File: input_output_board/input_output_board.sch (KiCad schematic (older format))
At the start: 20 parts, among them J1 Neutrik_NCJ6FA-H, J2 Neutrik_NCJ6FA-H, J3 Neutrik_NCJ6FA-H, J4 Neutrik_NCJ6FA-H, J5 AudioJack3, J6 Conn_02x05_Odd_Even, J7 Molex_SL_01x02_Male, J8 Molex_SL_01x02_Male, K1 G6S-2, K2 G6S-2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

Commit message: update input output board for headphone amp connections
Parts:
- added J6: Molex_SL_01x02_Male, Connector_Molex_SL:Molex_SL_A-70543-0001_1x02_P2.54mm_Vertical, symbol Connector_gkeeth:Molex_SL_01x02_Male
- added JP3, JP4: Jumper_NO_Small, Connector_PinHeader_2.54mm:PinHeader_1x02_P2.54mm_Vertical, symbol Device:Jumper_NO_Small
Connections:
- net labels added: headphone_cold, headphone_hot, headphone_select, main_cold, main_hot
- net labels removed: output_mute_select
- wire segments 141 -> 144
- no-connect marks 10 -> 8
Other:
- note added: "JP1 - JP4 optionally bypass K5\n\nTo hardwire main output:\nDNP K5, fit JP1 & JP3\n\nTo hardwire headphone output:\nDNP K5, fit JP2 & JP4"
- note added: "TODO\ncreate footprint for output jack\nmounting holes in corners?\npulldown resistors on J5?"
- note removed: "JP1 & JP2 optionally bypass K5\nif output relay is not required,\nDNP K5 and fit JP1 & JP2"
- note removed: "TODO\ncreate footprint for output jack\nmounting holes in corners?\nGND normally open terminals on K5? through resistor?"
- moved on the sheet: J6, J7

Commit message: Update layout of input/output board
- remove jumpers to bypass output relay. Jumper wires can be soldered
onto relay footprint instead.
- layout of output connectors complete
- still need to finalize output connector choice & placement
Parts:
- removed JP1, JP2, JP3, JP4: Jumper_NO_Small, Connector_PinHeader_2.54mm:PinHeader_1x02_P2.54mm_Vertical, symbol Device:Jumper_NO_Small
- J7, J8: footprint Connector_Molex_SL:Molex_SL_A-70543-0001_1x02_P2.54mm_Vertical -> Connector_Molex_SL:Molex_SL_A-70553-0001_1x02_P2.54mm_Horizontal
- J9: renamed from J6; footprint Connector_Molex_SL:Molex_SL_A-70543-0001_1x02_P2.54mm_Vertical -> Connector_Molex_SL:Molex_SL_A-70553-0001_1x02_P2.54mm_Horizontal
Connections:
- wire segments 144 -> 136
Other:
- note removed: "JP1 - JP4 optionally bypass K5\n\nTo hardwire main output:\nDNP K5, fit JP1 & JP3\n\nTo hardwire headphone output:\nDNP K5, fit JP2 & JP4"
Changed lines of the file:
@@
 F 0 "J7" H 6322 4674 50  0000 R CNN
 F 1 "Molex_SL_01x02_Male" H 6322 4583 50  0000 R CNN
-F 2 "Connector_Molex_SL:Molex_SL_A-70543-0001_1x02_P2.54mm_Vertical" H 6350 4700 50  0001 C CNN
+F 2 "Connector_Molex_SL:Molex_SL_A-70553-0001_1x02_P2.54mm_Horizontal" H 6350 4700 50  0001 C CNN
 F 3 "https://www.molex.com/pdm_docs/sd/705430001_sd.pdf" H 6350 4700 50  0001 C CNN
 F 4 "Molex" H 6350 4700 50  0001 C CNN "Manufacturer"
@@
 $EndComp
 $Comp
-L Connector_gkeeth:Molex_SL_01x02_Male J6
+L Connector_gkeeth:Molex_SL_01x02_Male J9
 U 1 1 5D8346C7
 P 10000 2400
-F 0 "J6" H 10108 2167 50  0000 C CNN
+F 0 "J9" H 10108 2167 50  0000 C CNN
 F 1 "Molex_SL_01x02_Male" H 10108 2076 50  0000 C CNN
-F 2 "Connector_Molex_SL:Molex_SL_A-70543-0001_1x02_P2.54mm_Vertical" H 10000 2400 50  0001 C CNN
+F 2 "Connector_Molex_SL:Molex_SL_A-70553-0001_1x02_P2.54mm_Horizontal" H 10000 2400 50  0001 C CNN
 F 3 "https://www.molex.com/pdm_docs/sd/705430001_sd.pdf" H 10000 2400 50  0001 C CNN
 F 4 "Molex" H 10000 2400 50  0001 C CNN "Manufacturer"
@@
 $EndComp
 $Comp
-L power_gkeeth:GNDRELAY #PWR?
+L power_gkeeth:GNDRELAY #PWR0101
 U 1 1 5D821EF0
 P 9000 1150
-F 0 "#PWR?" H 9000 900 50  0001 C CNN
+F 0 "#PWR0101" H 9000 900 50  0001 C CNN
 F 1 "GNDRELAY" H 9004 995 50  0000 C CNN
 F 2 "" H 9000 1150 50  0001 C CNN
 F 3 "" H 9000 1150 50  0001 C CNN
 	1    9000 1150
-	1    0    0    -1
-$EndComp
-$Comp
-L Device:Jumper_NO_Small JP2
-U 1 1 5D821EEA
-P 9600 3250
-F 0 "JP2" H 9600 3343 50  0000 C CNN
-F 1 "Jumper_NO_Small" H 9600 3371 50  0001 C CNN
-F 2 "Connector_PinHeader_2.54mm:PinHeader_1x02_P2.54mm_Vertical" H 9600 3250 50  0001 C CNN
-F 3 "~" H 9600 3250 50  0001 C CNN
-	1    9600 3250
-	1    0    0    -1
-$EndComp
-Text Notes 7550 3650 0    50   ~ 0
-JP1 - JP4 optionally bypass K5\n\nTo hardwire main output:\nDNP K5, fit JP1 & JP3\n\nTo hardwire headphone output:\nDNP K5, fit JP2 & JP4
-$Comp
-L Device:Jumper_NO_Small JP1
-U 1 1 5D821ED4
-P 9600 3050
-F 0 "JP1" H 9600 3150 50  0000 C CNN
-F 1 "Jumper_NO_Small" H 9600 3171 50  0001 C CNN
-F 2 "Connector_PinHeader_2.54mm:PinHeader_1x02_P2.54mm_Vertical" H 9600 3050 50  0001 C CNN
-F 3 "~" H 9600 3050 50  0001 C CNN
-	1    9600 3050
 	1    0    0    -1
 $EndComp
@@
 F 0 "J8" H 7072 1974 50  0000 R CNN
 F 1 "Molex_SL_01x02_Male" H 7072 1883 50  0000 R CNN
-F 2 "Connector_Molex_SL:Molex_SL_A-70543-0001_1x02_P2.54mm_Vertical" H 7100 2000 50  0001 C CNN
+F 2 "Connector_Molex_SL:Molex_SL_A-70553-0001_1x02_P2.54mm_Horizontal" H 7100 2000 50  0001 C CNN
 F 3 "https://www.molex.com/pdm_docs/sd/705430001_sd.pdf" H 7100 2000 50  0001 C CNN
 F 4 "Molex" H 7100 2000 50  0001 C CNN "Manufacturer"
@@
 	9750 1400 9800 1400
 Connection ~ 8750 1050
-$Comp
-L Device:Jumper_NO_Small JP3
-U 1 1 5DA7C338
-P 9600 3500
-F 0 "JP3" H 9600 3600 50  0000 C CNN
-F 1 "Jumper_NO_Small" H 9600 3621 50  0001 C CNN
-F 2 "Connector_PinHeader_2.54mm:PinHeader_1x02_P2.54mm_Vertical" H 9600 3500 50  0001 C CNN
-F 3 "~" H 9600 3500 50  0001 C CNN
-	1    9600 3500
-	1    0    0    -1
-$EndComp
-$Comp
-L Device:Jumper_NO_Small JP4
-U 1 1 5DA7C8D9
-P 9600 3700
-F 0 "JP4" H 9600 3793 50  0000 C CNN
-F 1 "Jumper_NO_Small" H 9600 3821 50  0001 C CNN
-F 2 "Connector_PinHeader_2.54mm:PinHeader_1x02_P2.54mm_Vertical" H 9600 3700 50  0001 C CNN
-F 3 "~" H 9600 3700 50  0001 C CNN
-	1    9600 3700
-	1    0    0    -1
-$EndComp
 Text Label 8800 1900 0    50   ~ 0
 main_hot
@@
 Wire Wire Line
 	9450 2400 9800 2400
-Wire Wire Line
-	9000 3050 9500 3050
-Wire Wire Line
-	9000 3250 9500 3250
-Wire Wire Line
-	9000 3500 9500 3500
-Wire Wire Line
-	9000 3700 9500 3700
-Wire Wire Line
-	10350 3050 9700 3050
-Wire Wire Line
-	10350 3250 9700 3250
-Wire Wire Line
-	10350 3500 9700 3500
-Wire Wire Line
-	10350 3700 9700 3700
-Text Label 9000 3050 0    50   ~ 0
-output_hot
-Text Label 9000 3500 0    50   ~ 0
-output_cold
-Text Label 9000 3250 0    50   ~ 0
-output_hot
-Text Label 9000 3700 0    50   ~ 0
-output_cold
-Text Label 10350 3050 2    50   ~ 0
-main_hot
-Text Label 10350 3250 2    50   ~ 0
-headphone_hot
-Text Label 10350 3500 2    50   ~ 0
-main_cold
-Text Label 10350 3700 2    50   ~ 0
-headphone_cold
 Wire Notes Line
 	10450 550  5950 550

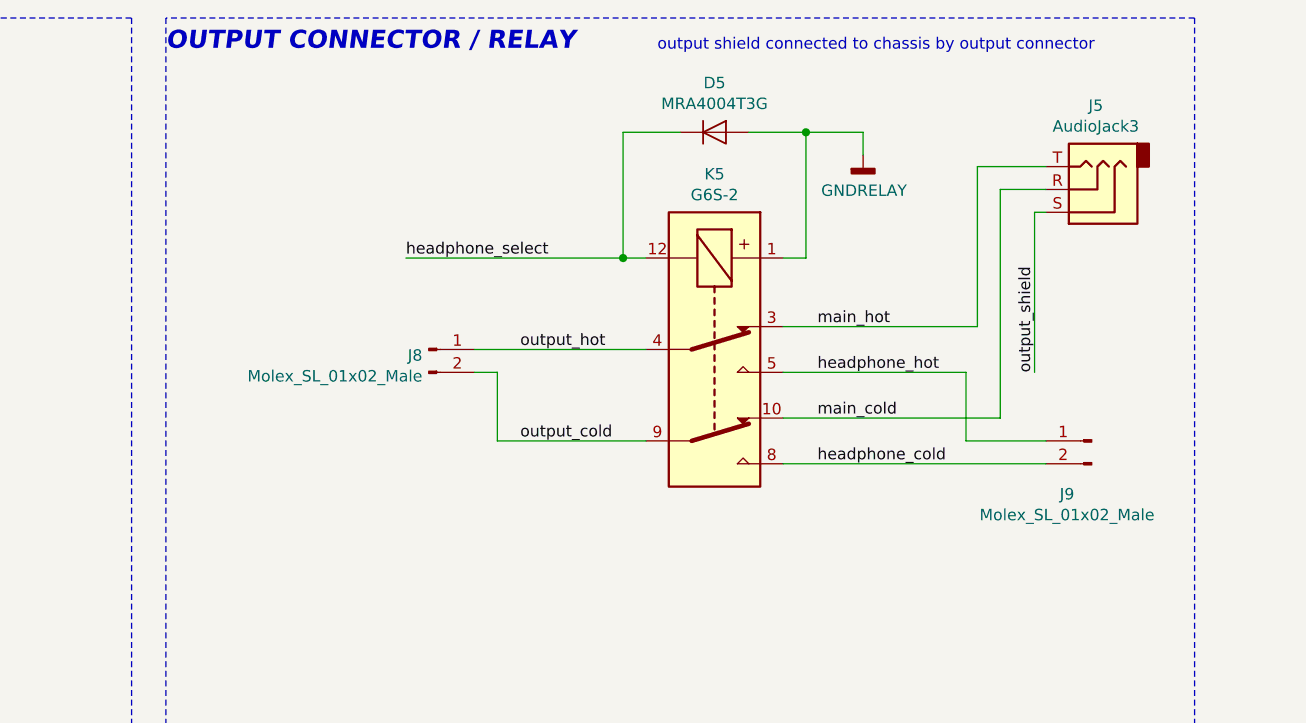
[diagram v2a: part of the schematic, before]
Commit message: update schematic & layout so output connector is same as input connectors
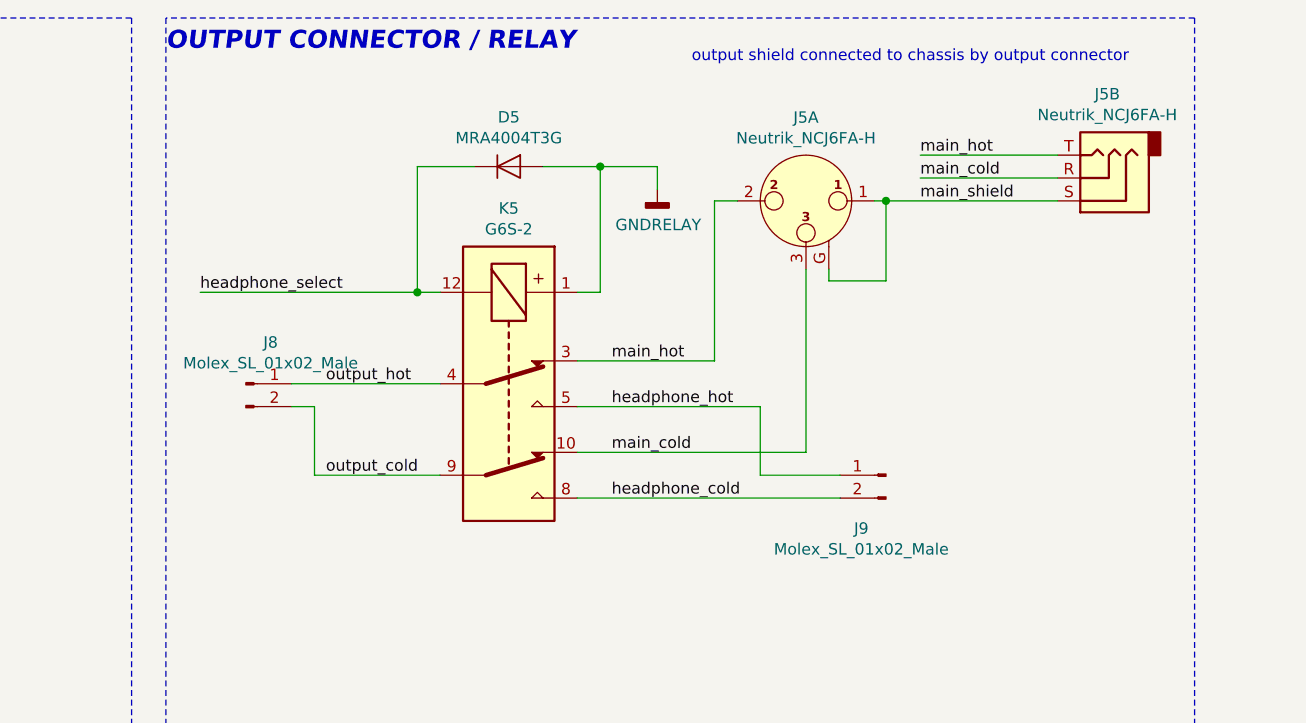
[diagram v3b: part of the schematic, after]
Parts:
- removed J5: AudioJack3, Connector_Audio:Jack_3.5mm_Neutrik_NMJ6HCD2_Horizontal, symbol Connector:AudioJack3
- added J5: Neutrik_NCJ6FA-H, Connector_Audio_gkeeth:Jack_Combo_Neutrik_NCJ6FA-H_Horizontal, symbol Connector_gkeeth:Neutrik_NCJ6FA-H
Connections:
- net main_cold: now also J5.3, J5.R
- net main_hot: now also J5.2, J5.T
- new net main_shield: J5.1, J5.G, J5.S
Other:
- moved on the sheet: D5, J8, J9, K5

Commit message: update schematic symbols to NCJ6FA-H-0 (no release tab), update footprints to project-local versions
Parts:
- J1, J2, J3, J4, J5: value Neutrik_NCJ6FA-H -> Neutrik_NCJ6FA-H-0; footprint Connector_Audio_gkeeth:Jack_Combo_Neutrik_NCJ6FA-H_Horizontal -> Connector_Audio_project:Jack_XLR-6.35mm_Neutrik_NCJ6FA-H-0_Horizontal; symbol Connector_gkeeth:Neutrik_NCJ6FA-H -> Connector_gkeeth:Neutrik_NCJ6FA-H-0
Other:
- note added: "TODO\nchange output jack to 6.35mm (not combo)\ncreate footprint for output jack\nmounting holes in corners?\npulldown resistors on J5?"
- note removed: "TODO\ncreate footprint for output jack\nmounting holes in corners?\npulldown resistors on J5?"
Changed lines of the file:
@@
 Tip: hot\nRing: cold\nSleeve: shield\n\n1: shield\n2: hot\n3: cold
 $Comp
-L Connector_gkeeth:Neutrik_NCJ6FA-H J2
+L Connector_gkeeth:Neutrik_NCJ6FA-H-0 J2
 U 1 1 5CAED56C
 P 2450 3450
 F 0 "J2" H 2450 3815 50  0000 C CNN
-F 1 "Neutrik_NCJ6FA-H" H 2450 3724 50  0000 C CNN
-F 2 "Connector_Audio_gkeeth:Jack_Combo_Neutrik_NCJ6FA-H_Horizontal" H 2450 3450 50  0001 C CNN
+F 1 "Neutrik_NCJ6FA-H-0" H 2450 3724 50  0000 C CNN
+F 2 "Connector_Audio_project:Jack_XLR-6.35mm_Neutrik_NCJ6FA-H-0_Horizontal" H 2450 3450 50  0001 C CNN
 F 3 "https://www.neutrik.com/media/8445/download/ncj6fa-v.pdf?v=1" H 2450 3450 50  0001 C CNN
 F 4 "Neutrik" H 2450 3450 50  0001 C CNN "Manufacturer"
@@
 $EndComp
 $Comp
-L Connector_gkeeth:Neutrik_NCJ6FA-H J2
+L Connector_gkeeth:Neutrik_NCJ6FA-H-0 J2
 U 2 1 5CAEF4BC
 P 1200 3350
 F 0 "J2" H 1182 2983 50  0000 C CNN
-F 1 "Neutrik_NCJ6FA-H" H 1182 3074 50  0000 C CNN
-F 2 "Connector_Audio_gkeeth:Jack_Combo_Neutrik_NCJ6FA-H_Horizontal" H 1200 3350 50  0001 C CNN
+F 1 "Neutrik_NCJ6FA-H-0" H 1182 3074 50  0000 C CNN
+F 2 "Connector_Audio_project:Jack_XLR-6.35mm_Neutrik_NCJ6FA-H-0_Horizontal" H 1200 3350 50  0001 C CNN
 F 3 "https://www.neutrik.com/media/8445/download/ncj6fa-v.pdf?v=1" H 1200 3350 50  0001 C CNN
 F 4 "Neutrik" H 1200 3350 50  0001 C CNN "Manufacturer"
@@
 Connection ~ 5000 5500
 $Comp
-L Connector_gkeeth:Neutrik_NCJ6FA-H J1
+L Connector_gkeeth:Neutrik_NCJ6FA-H-0 J1
 U 1 1 5CEE6A94
 P 2450 1700
 F 0 "J1" H 2450 2065 50  0000 C CNN
-F 1 "Neutrik_NCJ6FA-H" H 2450 1974 50  0000 C CNN
-F 2 "Connector_Audio_gkeeth:Jack_Combo_Neutrik_NCJ6FA-H_Horizontal" H 2450 1700 50  0001 C CNN
+F 1 "Neutrik_NCJ6FA-H-0" H 2450 1974 50  0000 C CNN
+F 2 "Connector_Audio_project:Jack_XLR-6.35mm_Neutrik_NCJ6FA-H-0_Horizontal" H 2450 1700 50  0001 C CNN
 F 3 "https://www.neutrik.com/media/8445/download/ncj6fa-v.pdf?v=1" H 2450 1700 50  0001 C CNN
 F 4 "Neutrik" H 2450 1700 50  0001 C CNN "Manufacturer"
@@
 $EndComp
 $Comp
-L Connector_gkeeth:Neutrik_NCJ6FA-H J1
+L Connector_gkeeth:Neutrik_NCJ6FA-H-0 J1
 U 2 1 5CEE74AE
 P 1200 1600
 F 0 "J1" H 1182 1233 50  0000 C CNN
-F 1 "Neutrik_NCJ6FA-H" H 1182 1324 50  0000 C CNN
-F 2 "Connector_Audio_gkeeth:Jack_Combo_Neutrik_NCJ6FA-H_Horizontal" H 1200 1600 50  0001 C CNN
+F 1 "Neutrik_NCJ6FA-H-0" H 1182 1324 50  0000 C CNN
+F 2 "Connector_Audio_project:Jack_XLR-6.35mm_Neutrik_NCJ6FA-H-0_Horizontal" H 1200 1600 50  0001 C CNN
 F 3 "https://www.neutrik.com/media/8445/download/ncj6fa-v.pdf?v=1" H 1200 1600 50  0001 C CNN
 F 4 "Neutrik" H 1200 1600 50  0001 C CNN "Manufacturer"
@@
 $EndComp
 $Comp
-L Connector_gkeeth:Neutrik_NCJ6FA-H J3
+L Connector_gkeeth:Neutrik_NCJ6FA-H-0 J3
 U 2 1 5CEE9005
 P 1200 5100
 F 0 "J3" H 1182 4733 50  0000 C CNN
-F 1 "Neutrik_NCJ6FA-H" H 1182 4824 50  0000 C CNN
-F 2 "Connector_Audio_gkeeth:Jack_Combo_Neutrik_NCJ6FA-H_Horizontal" H 1200 5100 50  0001 C CNN
+F 1 "Neutrik_NCJ6FA-H-0" H 1182 4824 50  0000 C CNN
+F 2 "Connector_Audio_project:Jack_XLR-6.35mm_Neutrik_NCJ6FA-H-0_Horizontal" H 1200 5100 50  0001 C CNN
 F 3 "https://www.neutrik.com/media/8445/download/ncj6fa-v.pdf?v=1" H 1200 5100 50  0001 C CNN
 F 4 "Neutrik" H 1200 5100 50  0001 C CNN "Manufacturer"
@@
 $EndComp
 $Comp
-L Connector_gkeeth:Neutrik_NCJ6FA-H J4
+L Connector_gkeeth:Neutrik_NCJ6FA-H-0 J4
 U 2 1 5CEE9880
 P 1200 6850
 F 0 "J4" H 1182 6483 50  0000 C CNN
-F 1 "Neutrik_NCJ6FA-H" H 1182 6574 50  0000 C CNN
-F 2 "Connector_Audio_gkeeth:Jack_Combo_Neutrik_NCJ6FA-H_Horizontal" H 1200 6850 50  0001 C CNN
+F 1 "Neutrik_NCJ6FA-H-0" H 1182 6574 50  0000 C CNN
+F 2 "Connector_Audio_project:Jack_XLR-6.35mm_Neutrik_NCJ6FA-H-0_Horizontal" H 1200 6850 50  0001 C CNN
 F 3 "https://www.neutrik.com/media/8445/download/ncj6fa-v.pdf?v=1" H 1200 6850 50  0001 C CNN
 F 4 "Neutrik" H 1200 6850 50  0001 C CNN "Manufacturer"
@@
 $EndComp
 $Comp
-L Connector_gkeeth:Neutrik_NCJ6FA-H J3
+L Connector_gkeeth:Neutrik_NCJ6FA-H-0 J3
 U 1 1 5CEEA018
 P 2450 5200
 F 0 "J3" H 2450 5565 50  0000 C CNN
-F 1 "Neutrik_NCJ6FA-H" H 2450 5474 50  0000 C CNN
-F 2 "Connector_Audio_gkeeth:Jack_Combo_Neutrik_NCJ6FA-H_Horizontal" H 2450 5200 50  0001 C CNN
+F 1 "Neutrik_NCJ6FA-H-0" H 2450 5474 50  0000 C CNN
+F 2 "Connector_Audio_project:Jack_XLR-6.35mm_Neutrik_NCJ6FA-H-0_Horizontal" H 2450 5200 50  0001 C CNN
 F 3 "https://www.neutrik.com/media/8445/download/ncj6fa-v.pdf?v=1" H 2450 5200 50  0001 C CNN
 F 4 "Neutrik" H 2450 5200 50  0001 C CNN "Manufacturer"
@@
 $EndComp
 $Comp
-L Connector_gkeeth:Neutrik_NCJ6FA-H J4
+L Connector_gkeeth:Neutrik_NCJ6FA-H-0 J4
 U 1 1 5CEEA75D
 P 2450 6950
 F 0 "J4" H 2450 7315 50  0000 C CNN
-F 1 "Neutrik_NCJ6FA-H" H 2450 7224 50  0000 C CNN
-F 2 "Connector_Audio_gkeeth:Jack_Combo_Neutrik_NCJ6FA-H_Horizontal" H 2450 6950 50  0001 C CNN
+F 1 "Neutrik_NCJ6FA-H-0" H 2450 7224 50  0000 C CNN
+F 2 "Connector_Audio_project:Jack_XLR-6.35mm_Neutrik_NCJ6FA-H-0_Horizontal" H 2450 6950 50  0001 C CNN
 F 3 "https://www.neutrik.com/media/8445/download/ncj6fa-v.pdf?v=1" H 2450 6950 50  0001 C CNN
 F 4 "Neutrik" H 2450 6950 50  0001 C CNN "Manufacturer"
@@
 input shield connected to chassis by input connector
 Text Notes 8200 6150 0    50   ~ 0
-TODO\ncreate footprint for output jack\nmounting holes in corners?\npulldown resistors on J5?
+TODO\nchange output jack to 6.35mm (not combo)\ncreate footprint for output jack\nmounting holes in corners?\npulldown resistors on J5?
 $Comp
 L power_gkeeth:GNDRELAY #PWR0102
@@
 	5000 5500 5000 7250
 $Comp
-L Connector_gkeeth:Neutrik_NCJ6FA-H J5
+L Connector_gkeeth:Neutrik_NCJ6FA-H-0 J5
 U 2 1 5D808DA8
 P 10050 1250
 F 0 "J5" H 10032 883 50  0000 C CNN
-F 1 "Neutrik_NCJ6FA-H" H 10032 974 50  0000 C CNN
-F 2 "Connector_Audio_gkeeth:Jack_Combo_Neutrik_NCJ6FA-H_Horizontal" H 10050 1250 50  0001 C CNN
+F 1 "Neutrik_NCJ6FA-H-0" H 10032 974 50  0000 C CNN
+F 2 "Connector_Audio_project:Jack_XLR-6.35mm_Neutrik_NCJ6FA-H-0_Horizontal" H 10050 1250 50  0001 C CNN
 F 3 "https://www.neutrik.com/media/8445/download/ncj6fa-v.pdf?v=1" H 10050 1250 50  0001 C CNN
 F 4 "Neutrik" H 10050 1250 50  0001 C CNN "Manufacturer"
@@
 $EndComp
 $Comp
-L Connector_gkeeth:Neutrik_NCJ6FA-H J5
+L Connector_gkeeth:Neutrik_NCJ6FA-H-0 J5
 U 1 1 5D807783
 P 8750 1350
 F 0 "J5" H 8750 1715 50  0000 C CNN
-F 1 "Neutrik_NCJ6FA-H" H 8750 1624 50  0000 C CNN
-F 2 "Connector_Audio_gkeeth:Jack_Combo_Neutrik_NCJ6FA-H_Horizontal" H 8750 1350 50  0001 C CNN
+F 1 "Neutrik_NCJ6FA-H-0" H 8750 1624 50  0000 C CNN
+F 2 "Connector_Audio_project:Jack_XLR-6.35mm_Neutrik_NCJ6FA-H-0_Horizontal" H 8750 1350 50  0001 C CNN
 F 3 "https://www.neutrik.com/media/8445/download/ncj6fa-v.pdf?v=1" H 8750 1350 50  0001 C CNN
 F 4 "Neutrik" H 8750 1350 50  0001 C CNN "Manufacturer"
